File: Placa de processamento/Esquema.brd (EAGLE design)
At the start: 145.1 x 71.2 mm, 11 parts

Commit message: Adicionado conexão LoRa
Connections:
- new net N$1: U$2.M0, U$4.2
- new net N$2: U$2.M1, U$4.1
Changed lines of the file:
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@@
 </elements>
 <signals>
+<signal name="N$1">
+<contactref element="U$2" pad="M0"/>
+<contactref element="U$4" pad="2"/>
+<wire x1="26.67" y1="19.05" x2="139.573" y2="47.752" width="0" layer="19" extent="1-1"/>
+</signal>
+<signal name="N$2">
+<contactref element="U$2" pad="M1"/>
+<contactref element="U$4" pad="1"/>
+<wire x1="26.67" y1="16.51" x2="139.573" y2="50.292" width="0" layer="19" extent="1-1"/>
+</signal>
 </signals>
 <mfgpreviewcolors>

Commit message: Ligado MPU ao ESP32
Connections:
- new net N$3: U$11.15, U$9.VCC
- new net N$4: U$11.12, U$9.GND
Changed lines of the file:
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@@
 <wire x1="26.67" y1="16.51" x2="139.573" y2="50.292" width="0" layer="19" extent="1-1"/>
+</signal>
+<signal name="N$3">
+<contactref element="U$9" pad="VCC"/>
+<contactref element="U$11" pad="15"/>
+<wire x1="36.8055" y1="32.9955" x2="96.53" y2="31.32" width="0" layer="19" extent="1-1"/>
+</signal>
+<signal name="N$4">
+<contactref element="U$9" pad="GND"/>
+<contactref element="U$11" pad="12"/>
+<wire x1="39.4055" y1="32.9955" x2="104.15" y2="31.32" width="0" layer="19" extent="1-1"/>
 </signal>
 </signals>

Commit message: Adicionado quase totas as conexões, falta aquelas relacionadas à alimentação (conectores JST)
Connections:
- new net N$10: U$11.19, U$8.MISO
- new net N$11: U$10.PR2, U$11.30
- new net N$13: U$11.17, U$2.RXD
- new net N$14: U$11.16, U$2.TXD
- new net N$5: U$11.15, U$3.TX
- new net N$6: U$11.4, U$3.RX
- new net N$7: U$11.5, U$8.CS
- new net N$8: U$11.23, U$8.MOSI
- new net N$9: U$11.18, U$8.CLK
- net N$1: now also U$1.SDA, U$11.21, U$9.SDA; no longer U$2.M0, U$4.2
- net N$2: now also U$1.SCL, U$11.22, U$9.SCL; no longer U$2.M1, U$4.1
- net N$3: now also U$1.3V0, U$11.1, U$3.VCC, U$8.3V3; no longer U$11.15
- net N$4: now also U$1.GND, U$11.2, U$2.GND, U$3.GND, U$8.GND; no longer U$11.12
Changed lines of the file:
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@@
 <signals>
 <signal name="N$1">
-<contactref element="U$2" pad="M0"/>
-<contactref element="U$4" pad="2"/>
-<wire x1="26.67" y1="19.05" x2="139.573" y2="47.752" width="0" layer="19" extent="1-1"/>
+<contactref element="U$11" pad="21"/>
+<contactref element="U$9" pad="SDA"/>
+<contactref element="U$1" pad="SDA"/>
+<wire x1="49.022" y1="6.35" x2="109.23" y2="6.55" width="0" layer="19" extent="1-1"/>
+<wire x1="44.6055" y1="32.9955" x2="49.022" y2="6.35" width="0" layer="19" extent="1-1"/>
 </signal>
 <signal name="N$2">
-<contactref element="U$2" pad="M1"/>
-<contactref element="U$4" pad="1"/>
-<wire x1="26.67" y1="16.51" x2="139.573" y2="50.292" width="0" layer="19" extent="1-1"/>
+<contactref element="U$9" pad="SCL"/>
+<contactref element="U$11" pad="22"/>
+<contactref element="U$1" pad="SCL"/>
+<wire x1="43.942" y1="6.35" x2="111.77" y2="6.55" width="0" layer="19" extent="1-1"/>
+<wire x1="42.0055" y1="32.9955" x2="43.942" y2="6.35" width="0" layer="19" extent="1-1"/>
 </signal>
 <signal name="N$3">
 <contactref element="U$9" pad="VCC"/>
-<contactref element="U$11" pad="15"/>
-<wire x1="36.8055" y1="32.9955" x2="96.53" y2="31.32" width="0" layer="19" extent="1-1"/>
+<contactref element="U$11" pad="1"/>
+<contactref element="U$1" pad="3V0"/>
+<contactref element="U$3" pad="VCC"/>
+<contactref element="U$8" pad="3V3"/>
+<wire x1="70.05" y1="38.1" x2="132.09" y2="31.32" width="0" layer="19" extent="1-1"/>
+<wire x1="36.8055" y1="32.9955" x2="70.05" y2="38.1" width="0" layer="19" extent="1-1"/>
+<wire x1="30.099" y1="33.02" x2="36.8055" y2="32.9955" width="0" layer="19" extent="1-1"/>
+<wire x1="38.862" y1="6.35" x2="36.8055" y2="32.9955" width="0" layer="19" extent="1-1"/>
 </signal>
 <signal name="N$4">
+<contactref element="U$11" pad="2"/>
 <contactref element="U$9" pad="GND"/>
-<contactref element="U$11" pad="12"/>
-<wire x1="39.4055" y1="32.9955" x2="104.15" y2="31.32" width="0" layer="19" extent="1-1"/>
+<contactref element="U$1" pad="GND"/>
+<contactref element="U$3" pad="GND"/>
+<contactref element="U$8" pad="GND"/>
+<contactref element="U$2" pad="GND"/>
+<wire x1="129.55" y1="31.32" x2="139.573" y2="62.992" width="0" layer="19" extent="1-1"/>
+<wire x1="77.67" y1="38.1" x2="129.55" y2="31.32" width="0" layer="19" extent="1-1"/>
+<wire x1="39.4055" y1="32.9955" x2="77.67" y2="38.1" width="0" layer="19" extent="1-1"/>
+<wire x1="30.099" y1="45.72" x2="39.4055" y2="32.9955" width="0" layer="19" extent="1-1"/>
+<wire x1="41.402" y1="6.35" x2="39.4055" y2="32.9955" width="0" layer="19" extent="1-1"/>
+</signal>
+<signal name="N$5">
+<contactref element="U$3" pad="TX"/>
+<contactref element="U$11" pad="15"/>
+<wire x1="75.13" y1="38.1" x2="96.53" y2="31.32" width="0" layer="19" extent="1-1"/>
+</signal>
+<signal name="N$6">
+<contactref element="U$11" pad="4"/>
+<contactref element="U$3" pad="RX"/>
+<wire x1="72.59" y1="38.1" x2="124.47" y2="31.32" width="0" layer="19" extent="1-1"/>
+</signal>
+<signal name="N$7">
+<contactref element="U$11" pad="5"/>
+<contactref element="U$8" pad="CS"/>
+<wire x1="30.099" y1="35.56" x2="121.93" y2="31.32" width="0" layer="19" extent="1-1"/>
+</signal>
+<signal name="N$8">
+<contactref element="U$8" pad="MOSI"/>
+<contactref element="U$11" pad="23"/>
+<wire x1="30.099" y1="38.1" x2="114.31" y2="6.55" width="0" layer="19" extent="1-1"/>
+</signal>
+<signal name="N$9">
+<contactref element="U$8" pad="CLK"/>
+<contactref element="U$11" pad="18"/>
+<wire x1="30.099" y1="40.64" x2="101.61" y2="6.55" width="0" layer="19" extent="1-1"/>
+</signal>
+<signal name="N$10">
+<contactref element="U$8" pad="MISO"/>
+<contactref element="U$11" pad="19"/>
+<wire x1="30.099" y1="43.18" x2="104.15" y2="6.55" width="0" layer="19" extent="1-1"/>
+</signal>
+<signal name="N$11">
+<contactref element="U$10" pad="PR2"/>
+<contactref element="U$11" pad="30"/>
+<wire x1="8.818" y1="21.313" x2="132.09" y2="6.55" width="0" layer="19" extent="1-1"/>
+</signal>
+<signal name="N$13">
+<contactref element="U$2" pad="RXD"/>
+<contactref element="U$11" pad="17"/>
+<wire x1="99.07" y1="6.55" x2="139.573" y2="52.832" width="0" layer="19" extent="1-1"/>
+</signal>
+<signal name="N$14">
+<contactref element="U$2" pad="TXD"/>
+<contactref element="U$11" pad="16"/>
+<wire x1="96.53" y1="6.55" x2="139.573" y2="55.372" width="0" layer="19" extent="1-1"/>
 </signal>
 </signals>

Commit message: Roteamento da placa
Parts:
- added IC1: (no value), v-reg:78LXX
- moved U$2 16.6 mm to (121.9, 73.7)
- moved U$10 14.5 mm to (3.81, 30.5)
- moved U$4 7.73 mm to (25.4, 25.4)
- moved U$6 7.73 mm to (17.8, 25.4)
- moved U$3 5.68 mm to (71.1, 26.7), turned to 0 degrees
- moved U$11 5.39 mm to (105.4, 21.6)
- moved U$8 5.24 mm to (21.6, 44.5)
- moved U$1 5.24 mm to (43.6, 19.8)
- moved U$7 5.24 mm to (25.4, 12.7), turned to 270 degrees
- moved U$5 5.24 mm to (17.8, 12.7), turned to 270 degrees
- moved U$9 5.24 mm to (44.5, 48.3)
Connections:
- new net GND: U$11.29, U$7.2
- new net N$12: IC1.OUT, U$2.VCC
- new net N$15: U$11.9, U$8.CLK
- new net N$16: U$11.10, U$8.MISO
- new net N$19: U$11.28, U$6.1
- new net N$20: U$11.27, U$6.2
- new net N$21: U$11.26, U$4.1
- new net N$22: U$11.19, U$5.1
- new net N$23: U$11.20, U$5.2
- new net V_BATTERY: U$10.PL3, U$10.PR3, U$7.1
- net N$1: now also U$11.11; no longer U$11.21
- net N$10: now also U$11.22, U$2.M1; no longer U$11.19, U$8.MISO
- net N$11: now also U$11.21, U$2.M0; no longer U$10.PR2, U$11.30
- net N$13: now also U$11.8, U$8.CS; no longer U$11.17, U$2.RXD
- net N$14: now also U$11.15, U$8.MOSI; no longer U$11.16, U$2.TXD
- net N$2: now also U$11.14; no longer U$11.22
- net N$3: now also U$4.2
- net N$4: now also IC1.GND
- net N$5: now also U$11.5, U$3.RX; no longer U$11.15, U$3.TX
- net N$6: now also U$11.3, U$3.TX; no longer U$11.4, U$3.RX
- net N$7: now also IC1.IN, U$10.PL2, U$10.PR2, U$11.30; no longer U$11.5, U$8.CS
- net N$8: now also U$11.7, U$2.TXD; no longer U$11.23, U$8.MOSI
- net N$9: now also U$11.6, U$2.RXD; no longer U$11.18, U$8.CLK
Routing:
- net N$7: track 0.00 -> 220.8 mm, vias 0 -> 2
- net N$20: track 0.00 -> 130.2 mm, vias 0 -> 2
- net N$19: track 0.00 -> 116.0 mm, vias 0 -> 2
- net N$3: track 0.00 -> 109.8 mm
- net N$21: track 0.00 -> 100.5 mm, vias 0 -> 2
- net N$11: track 0.00 -> 94.8 mm
- net N$2: track 0.00 -> 94.7 mm
- net N$23: track 0.00 -> 93.0 mm
- net N$13: track 0.00 -> 89.9 mm
- net N$22: track 0.00 -> 88.7 mm
- net N$15: track 0.00 -> 88.5 mm, vias 0 -> 2
- net N$1: track 0.00 -> 87.1 mm
- net N$16: track 0.00 -> 85.7 mm, vias 0 -> 2
- net N$12: track 0.00 -> 81.8 mm
- net N$10: track 0.00 -> 75.3 mm
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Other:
- board size 145.1 x 71.2 mm -> 145.1 x 90.2 mm

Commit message: Componentes de biblioteca atualizados
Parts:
- moved U$10 14.5 mm to (7.62, 16.5)
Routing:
- net N$7: track 220.8 -> 222.5 mm
- net V_BATTERY: track 22.4 -> 20.9 mm
- net N$9: track 50.8 -> 49.6 mm
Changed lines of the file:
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@@
 </autorouter>
 <elements>
-<element name="U$1" library="CRD" library_urn="urn:adsk.eagle:library:39051337" package="BMP390_FOOTPRINT" package3d_urn="urn:adsk.eagle:package:40965124/4" value="BMP390V1" x="43.561" y="19.812" smashed="yes"/>
-<element name="U$10" library="CRD" library_urn="urn:adsk.eagle:library:39051337" package="PRESSION_BUTTON_FOOTPRINT" package3d_urn="urn:adsk.eagle:package:43483815/1" value="PRESSION_BUTTON" x="3.81" y="30.48" smashed="yes" rot="R270"/>
-<element name="U$2" library="CRD" library_urn="urn:adsk.eagle:library:39051337" package="E22-400T30D_FOOTPRINT" package3d_urn="urn:adsk.eagle:package:40965099/3" value="E22-400T30D" x="121.92" y="73.66" smashed="yes" rot="R180"/>
-<element name="U$3" library="CRD" library_urn="urn:adsk.eagle:library:39051337" package="GPS_MODULE_FOOTPRINT" package3d_urn="urn:adsk.eagle:package:39608400/4" value="GPS_MODULE" x="71.12" y="26.67" smashed="yes"/>
+<element name="U$1" library="CRD" library_urn="urn:adsk.eagle:library:39051337" package="BMP390_FOOTPRINT" package3d_urn="urn:adsk.eagle:package:40965124/5" value="BMP390V1" x="43.561" y="19.812" smashed="yes"/>
+<element name="U$10" library="CRD" library_urn="urn:adsk.eagle:library:39051337" package="PRESSION_BUTTON_FOOTPRINT" package3d_urn="urn:adsk.eagle:package:43483815/3" value="PRESSION_BUTTON" x="7.62" y="16.51" smashed="yes" rot="R270"/>
+<element name="U$2" library="CRD" library_urn="urn:adsk.eagle:library:39051337" package="E22-400T30D_FOOTPRINT" package3d_urn="urn:adsk.eagle:package:40965099/4" value="E22-400T30D" x="121.92" y="73.66" smashed="yes" rot="R180"/>
+<element name="U$3" library="CRD" library_urn="urn:adsk.eagle:library:39051337" package="GPS_MODULE_FOOTPRINT" package3d_urn="urn:adsk.eagle:package:39608400/5" value="GPS_MODULE" x="71.12" y="26.67" smashed="yes"/>
 <element name="U$4" library="CRD" library_urn="urn:adsk.eagle:library:39051337" package="JST2.54X2P_FOOTPRINT" package3d_urn="urn:adsk.eagle:package:39191967/2" value="JST2.54X2P" x="25.4" y="25.4" smashed="yes" rot="R90"/>
 <element name="U$5" library="CRD" library_urn="urn:adsk.eagle:library:39051337" package="JST2.54X2P_FOOTPRINT" package3d_urn="urn:adsk.eagle:package:39191967/2" value="JST2.54X2P" x="17.78" y="12.7" smashed="yes" rot="R270"/>
@@
 <element name="U$7" library="CRD" library_urn="urn:adsk.eagle:library:39051337" package="JST2.54X2P_FOOTPRINT" package3d_urn="urn:adsk.eagle:package:39191967/2" value="JST2.54X2P" x="25.4" y="12.7" smashed="yes" rot="R270"/>
 <element name="U$8" library="CRD" library_urn="urn:adsk.eagle:library:39051337" package="MICROSD_SMALL_READER_FOOTPRINT" package3d_urn="urn:adsk.eagle:package:44017969/2" value="MICROSD_SMALL_READER" x="21.59" y="44.45" smashed="yes" rot="R180"/>
-<element name="U$9" library="CRD" library_urn="urn:adsk.eagle:library:39051337" package="MPU6050_FOOTPRINT" package3d_urn="urn:adsk.eagle:package:39029071/7" value="MPU6050V1" x="44.45" y="48.26" smashed="yes"/>
+<element name="U$9" library="CRD" library_urn="urn:adsk.eagle:library:39051337" package="MPU6050_FOOTPRINT" package3d_urn="urn:adsk.eagle:package:39029071/8" value="MPU6050V1" x="44.45" y="48.26" smashed="yes"/>
 <element name="U$11" library="ESP32-DEVKITV1" library_urn="urn:adsk.eagle:library:44018017" package="ESP32-DEVKITV1" package3d_urn="urn:adsk.eagle:package:44018021/1" value="ESP32DEVKITV1" x="105.41" y="21.59" smashed="yes" rot="R180">
 <attribute name="NAME" x="129.54" y="7.62" size="1.27" layer="21" rot="R180"/>
@@
 <contactref element="U$2" pad="TXD"/>
 <contactref element="U$11" pad="7"/>
-<wire x1="113.04" y1="35.13" x2="112.99" y2="35.153721875" width="1.25" layer="16"/>
 <wire x1="138.303" y1="71.882" x2="138.2" y2="71.985" width="1.5" layer="16"/>
 <wire x1="126.31704375" y1="71.985" x2="138.2" y2="71.985" width="1.5" layer="16"/>
 <wire x1="112.99" y1="58.65795625" x2="126.31704375" y2="71.985" width="1.5" layer="16"/>
 <wire x1="112.99" y1="35.153721875" x2="112.99" y2="58.65795625" width="1.5" layer="16"/>
+<wire x1="112.99" y1="35.153721875" x2="113.04" y2="35.13" width="0" layer="19" extent="16-16"/>
 </signal>
 <signal name="N$9">
@@
 <wire x1="128.143" y1="69.342" x2="115.57" y2="56.769" width="1.5" layer="16"/>
 <wire x1="115.57" y1="56.769" x2="115.57" y2="36.83" width="1.5" layer="16"/>
-<wire x1="115.57" y1="35.615" x2="115.57" y2="36.83" width="1.5" layer="16"/>
-<wire x1="115.57" y1="36.83" x2="115.58" y2="36.82" width="1.5" layer="16"/>
-<wire x1="115.58" y1="36.82" x2="115.58" y2="35.13" width="1.5" layer="16"/>
+<wire x1="115.58" y1="36.82" x2="115.57" y2="36.83" width="1.5" layer="16"/>
+<wire x1="115.57" y1="36.83" x2="115.57" y2="35.14" width="1.5" layer="16"/>
+<wire x1="115.57" y1="35.14" x2="115.58" y2="35.13" width="1.5" layer="16"/>
 </signal>
 <signal name="N$10">
@@
 <wire x1="132.28" y1="10.36" x2="128.28" y2="10.36" width="1.5" layer="16"/>
 <wire x1="137.16" y1="15.24" x2="132.28" y2="10.36" width="1.5" layer="16"/>
-<contactref element="U$10" pad="PL2"/>
 <wire x1="25.4" y1="54.61" x2="55.88" y2="54.61" width="1.5" layer="16"/>
 <wire x1="55.88" y1="54.61" x2="59.69" y2="54.61" width="1.5" layer="16"/>
@@
 <wire x1="95.25" y1="60.96" x2="99.06" y2="57.15" width="1.5" layer="16"/>
 <wire x1="95.25" y1="60.96" x2="62.23" y2="60.96" width="1.5" layer="16"/>
-<wire x1="14.323" y1="25.753" x2="12.206371875" y2="23.636371875" width="1.5" layer="16"/>
-<wire x1="14.323" y1="25.753" x2="14.323" y2="43.533" width="1.5" layer="16"/>
+<wire x1="14.323" y1="25.753" x2="14.323" y2="26.67" width="1.5" layer="16"/>
+<wire x1="14.323" y1="26.67" x2="14.323" y2="43.533" width="1.5" layer="16"/>
 <wire x1="55.88" y1="54.61" x2="62.23" y2="60.96" width="1.5" layer="16"/>
 <wire x1="59.69" y1="54.61" x2="63.5" y2="58.42" width="1.5" layer="16"/>
 <wire x1="63.5" y1="58.42" x2="64.77" y2="58.42" width="1.5" layer="16"/>
 <contactref element="U$10" pad="PR2"/>
-<wire x1="12.206371875" y1="23.636371875" x2="9.0794375" y2="23.636371875" width="1.5" layer="16"/>
-<wire x1="5.6504375" y1="23.636371875" x2="9.0794375" y2="23.636371875" width="1.5" layer="16"/>
+<contactref element="U$10" pad="PL2"/>
+<wire x1="6.318" y1="21.313" x2="8.818" y2="21.313" width="1.5" layer="16"/>
+<wire x1="8.818" y1="21.313" x2="9.095" y2="21.59" width="1.5" layer="16"/>
+<wire x1="9.095" y1="21.59" x2="12.7" y2="21.59" width="1.5" layer="16"/>
+<wire x1="12.7" y1="21.59" x2="14.323" y2="23.213" width="1.5" layer="16"/>
+<wire x1="14.323" y1="23.213" x2="14.323" y2="25.753" width="1.5" layer="16"/>
 </signal>
 <signal name="N$12">
@@
 <contactref element="U$7" pad="1"/>
 <wire x1="23.59" y1="13.97" x2="25.4" y2="13.97" width="1.5" layer="16"/>
-<wire x1="17.158796875" y1="20.401203125" x2="23.59" y2="13.97" width="1.5" layer="16"/>
 <contactref element="U$10" pad="PL3"/>
 <contactref element="U$10" pad="PR3"/>
-<wire x1="5.6214" y1="20.401203125" x2="9.0504" y2="20.401203125" width="1.5" layer="16"/>
-<wire x1="9.0504" y1="20.401203125" x2="17.158796875" y2="20.401203125" width="1.5" layer="16"/>
+<wire x1="19.415" y1="18.145" x2="23.59" y2="13.97" width="1.5" layer="16"/>
+<wire x1="6.318" y1="18.313" x2="8.818" y2="18.313" width="1.5" layer="16"/>
+<wire x1="8.818" y1="18.313" x2="19.247" y2="18.313" width="1.5" layer="16"/>
+<wire x1="19.247" y1="18.313" x2="19.415" y2="18.145" width="1.5" layer="16"/>
 </signal>
 <signal name="N$19">
@@
 <wire x1="67.31" y1="21.59" x2="62.23" y2="26.67" width="1.5" layer="1"/>
 <wire x1="120.66" y1="15.23" x2="120.66" y2="13.98" width="1.5" layer="1"/>
-<wire x1="120.66" y1="13.98" x2="120.65" y2="13.97" width="1.5" layer="1"/>
 <via x="120.66" y="13.98" extent="1-16" drill="0.7" diameter="1.3"/>
 <wire x1="120.66" y1="13.98" x2="120.66" y2="10.36" width="1.5" layer="16"/>

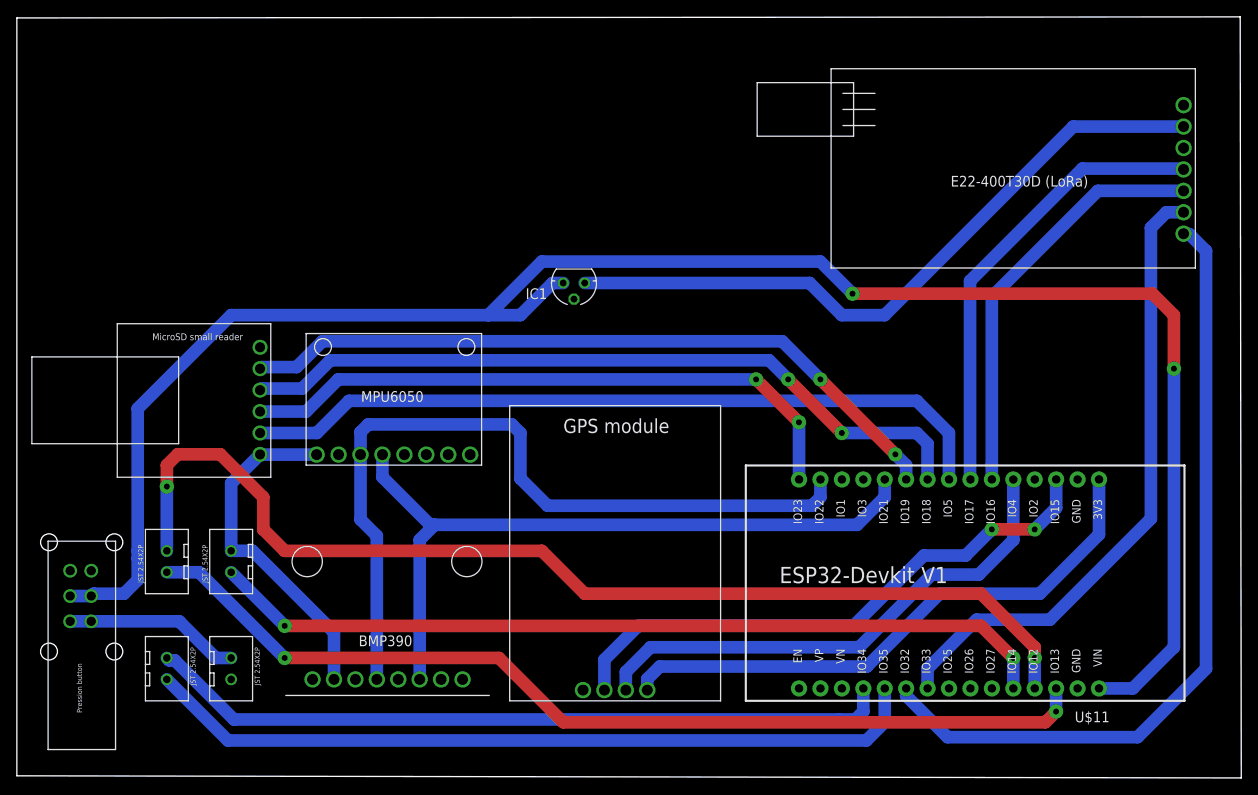
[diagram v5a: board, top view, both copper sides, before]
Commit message: Ajustes em trilhas, adicionado furos, ajustado dimensões
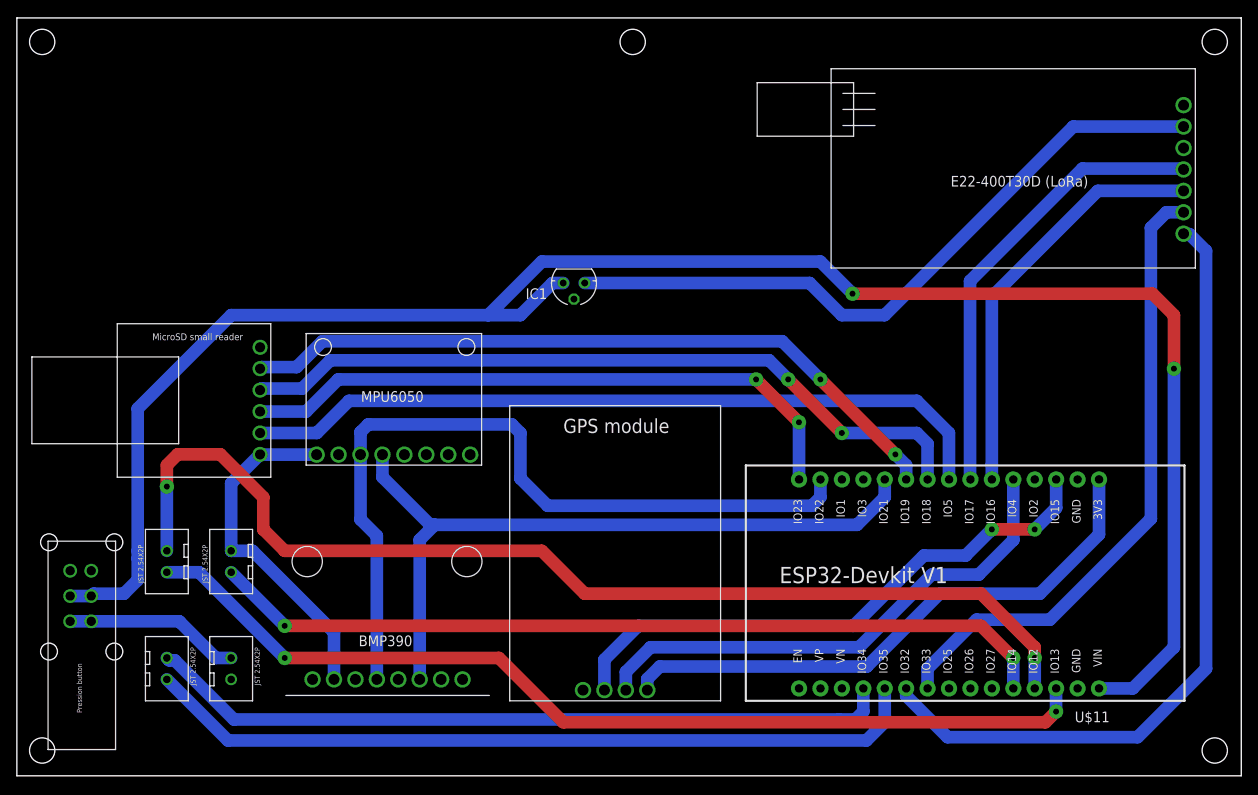
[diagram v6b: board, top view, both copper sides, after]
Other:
- board size 145.1 x 90.2 mm -> 145.1 x 89.8 mm
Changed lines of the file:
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@@
 <setting verticaltext="up"/>
 </settings>
-<grid distance="50" unitdist="mil" unit="mm" style="lines" multiple="1" display="yes" altdistance="5" altunitdist="mil" altunit="mm"/>
+<grid distance="1" unitdist="mm" unit="mm" style="lines" multiple="1" display="yes" altdistance="0.1" altunitdist="mm" altunit="mm"/>
 <layers>
 <layer number="1" name="Top" color="4" fill="1" visible="yes" active="yes"/>
@@
 <layer number="43" name="vRestrict" color="2" fill="10" visible="yes" active="yes"/>
 <layer number="44" name="Drills" color="7" fill="1" visible="no" active="yes"/>
-<layer number="45" name="Holes" color="7" fill="1" visible="no" active="yes"/>
+<layer number="45" name="Holes" color="7" fill="1" visible="yes" active="yes"/>
 <layer number="46" name="Milling" color="3" fill="1" visible="no" active="yes"/>
 <layer number="47" name="Measures" color="7" fill="1" visible="yes" active="yes"/>
@@
 <board>
 <plain>
-<wire x1="0" y1="0" x2="145.141" y2="-0.254" width="0" layer="20"/>
-<wire x1="145.141" y1="-0.254" x2="145.014" y2="89.967" width="0" layer="20"/>
-<wire x1="145.014" y1="89.967" x2="0" y2="89.84" width="0" layer="20"/>
+<wire x1="0" y1="0" x2="145.141" y2="0" width="0" layer="20"/>
+<wire x1="145.141" y1="0" x2="145.141" y2="89.84" width="0" layer="20"/>
+<wire x1="145.141" y1="89.84" x2="0" y2="89.84" width="0" layer="20"/>
 <wire x1="0" y1="89.84" x2="0" y2="0" width="0" layer="20"/>
 <dimension x1="0" y1="-3.81" x2="145.161" y2="-3.81" x3="72.5805" y3="-7.62" textsize="1.778" layer="27"/>
 <dimension x1="-2.54" y1="0" x2="-2.54" y2="90.17" x3="-5.08" y3="45.085" textsize="1.778" layer="47"/>
+<hole x="142" y="87" drill="3"/>
+<hole x="142" y="3" drill="3"/>
+<hole x="3" y="3" drill="3"/>
+<hole x="3" y="87" drill="3"/>
+<hole x="73" y="87" drill="3"/>
 </plain>
 <attributes>
